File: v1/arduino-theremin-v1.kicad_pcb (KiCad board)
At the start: 2 copper layers, 71.1 x 53.3 mm, 36 parts, among them SW2 ON-OFF-ON SWITCH, U1 Arduino_Uno_R3_Shield

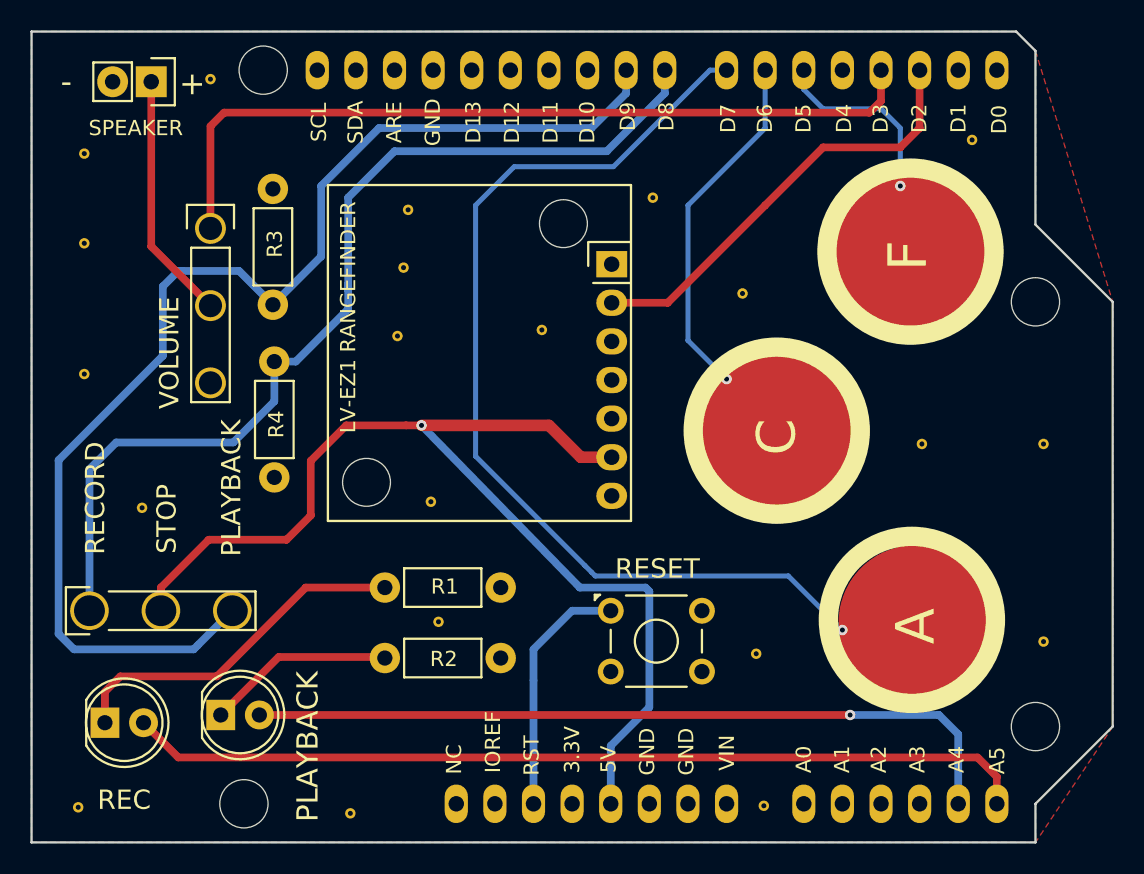
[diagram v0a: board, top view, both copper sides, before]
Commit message: v1.3, based on wickerlib, fixes the reversed rangefinder. Ordered from OSH Park.
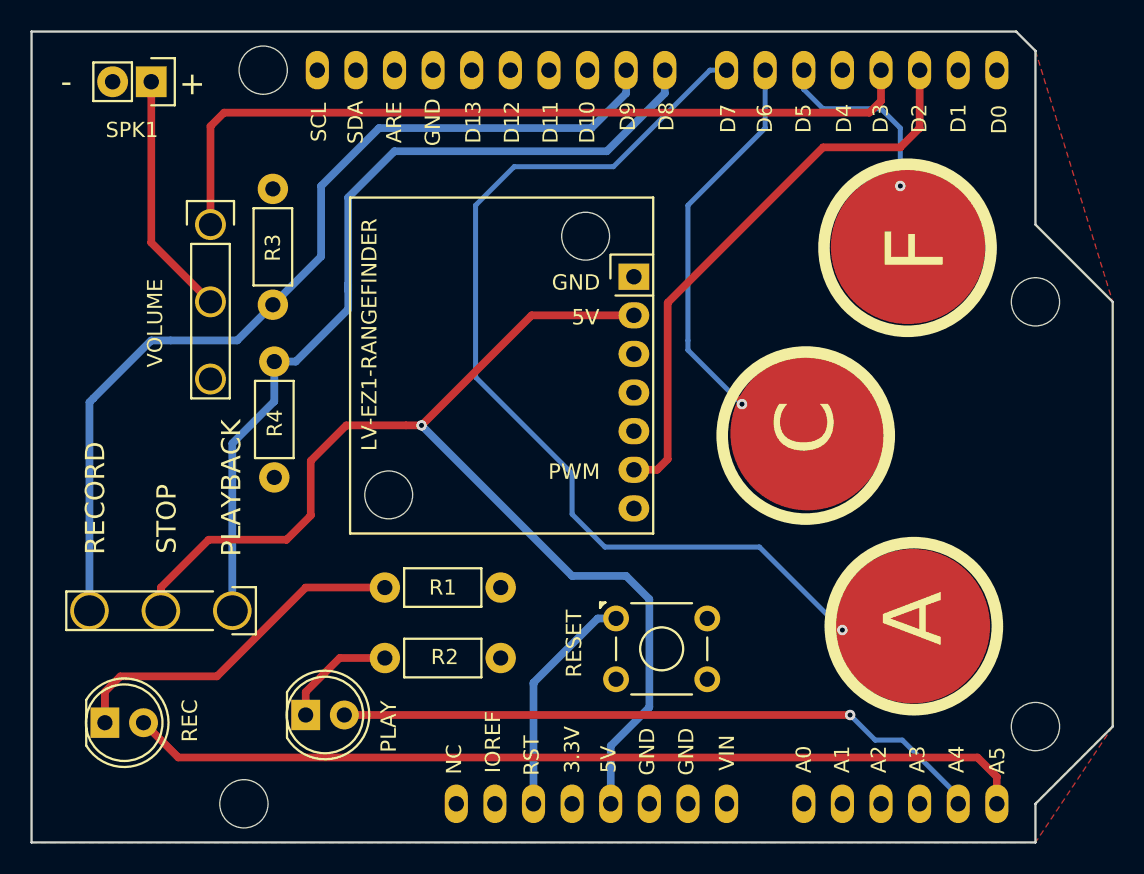
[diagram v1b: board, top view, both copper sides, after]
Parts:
- removed the A at (145.8, 103.6)
- removed the C at (136.7, 90.9)
- removed the F at (145.3, 79.2)
- removed LV-EZ1 RANGEFINDER: LV-EZ1 RANGEFINDER, Wicker_Modules:LV_EZ1_Rangefinder
- removed PLAYBACK: PLAYBACK, LEDs:LED-5MM
- removed the REC at (92.5, 110.2)
- removed REF** (x21): Via_13mil, Wicker_Buttons_Switches:Via_13mil
- removed the RESET at (125.7, 102.9)
- removed SPEAKER: SPEAKER, Pin_Headers:Pin_Header_Straight_1x02
- removed SW2: ON-OFF-ON SWITCH, Wicker_Buttons_Switches:ESwitch_Series100_SPDT
- removed the VOLUME at (99.4, 77.7)
- added A: KEY1, Wickerlib:CAPSENSE-CIRCLE-D10, F.Cu at (145.6, 103.9)
- added C: KEY2, Wickerlib:CAPSENSE-CIRCLE-D10, F.Cu at (138.7, 91.2)
- added F: KEY3, Wickerlib:CAPSENSE-CIRCLE-D10, F.Cu at (145.3, 78.9)
- added LV-EZ1-RANGEFINDER: LV-EZ1-RANGEFINDER, Wickerlib:LV_EZ1_Rangefinder, F.Cu at (108.6, 97.8)
- added PLAY: PLAYBACK, Wickerlib:LED-5MM-2PIN, F.Cu at (105.7, 109.7)
- added REC: RECORD, Wickerlib:LED-5MM-2PIN, F.Cu at (92.5, 110.2)
- added RESET: B3F-1000, Wickerlib:SW-B3F-10XX, F.Cu at (126.1, 103.4)
- added S1: RECORD-OFF-PLAYBACK, Wickerlib:SW-100SP3, F.Cu at (100.8, 102.9)
- added SPK1: SPEAKER-8OHM-23MM-ROUND-2PIN, Wickerlib:Pin_Header_Straight_1x02, F.Cu at (95.5, 68.1)
- added VOLUME: 10K, Wickerlib:P160-TRIMPOT, F.Cu at (99.4, 77.5)
- R1, R2, R3, R4: footprint Resistors_ThroughHole:Resistor_Horizontal_RM7mm -> Wickerlib:Resistor_Horizontal_RM7mm
- U1: value Arduino_Uno_R3_Shield -> ARDUINO-UNO-SHIELD; footprint Wicker_Shields:Arduino_Uno_R3_No_ICSP -> Wickerlib:ARDU-UNOSHIELD
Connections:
- R3 pad 1: /D8_BTN_PLAYBACK -> /D9_BTN_RECORD
- R4 pad 1: /D9_BTN_RECORD -> /D8_BTN_PLAYBACK
- U1 pad A5: /A5_ON_LED -> /A5_RECORD_LED
- U1 pad D8: /D9_BTN_RECORD -> /D8_BTN_PLAYBACK
- U1 pad D9: /D8_BTN_PLAYBACK -> /D9_BTN_RECORD
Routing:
- net /A5_RECORD_LED: track 0.00 -> 59.4 mm
- net /A5_ON_LED: track 59.4 -> 0.00 mm
- net /D8_BTN_PLAYBACK: track 80.4 -> 56.7 mm
- net /D2_PWM: track 28.8 -> 37.9 mm
- net /A4_PLAYBACK_LED: track 51.1 -> 43.1 mm
- net Net-(LED2-Pad1): track 12.4 -> 7.73 mm
- net /D9_BTN_RECORD: track 65.1 -> 61.7 mm
- net /D6_KEY2: track 28.1 -> 31.1 mm
- net +5V: track 73.5 -> 76.4 mm
- net /D7_KEY1: track 70.3 -> 68.8 mm
- net /RESET: track 16.3 -> 15.1 mm
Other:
- board text added: "5V"
- board text added: "Arduino Theremin Shield Demo Board v1.3 OSH Park 2016"
- board text added: "GND"
- board text added: "PWM"
- board text removed: "Arduino Theremin Shield Demo Board v1.1 OSH Park 2016"
